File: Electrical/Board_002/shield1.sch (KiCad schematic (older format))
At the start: 12 parts, among them J1 Conn_01x02, J2 RJ45, P1 Power, P2 Analog, P3 Digital, P4 Digital, P5 CONN_01X01, P6 CONN_01X01, P7 CONN_01X01, P8 CONN_01X01

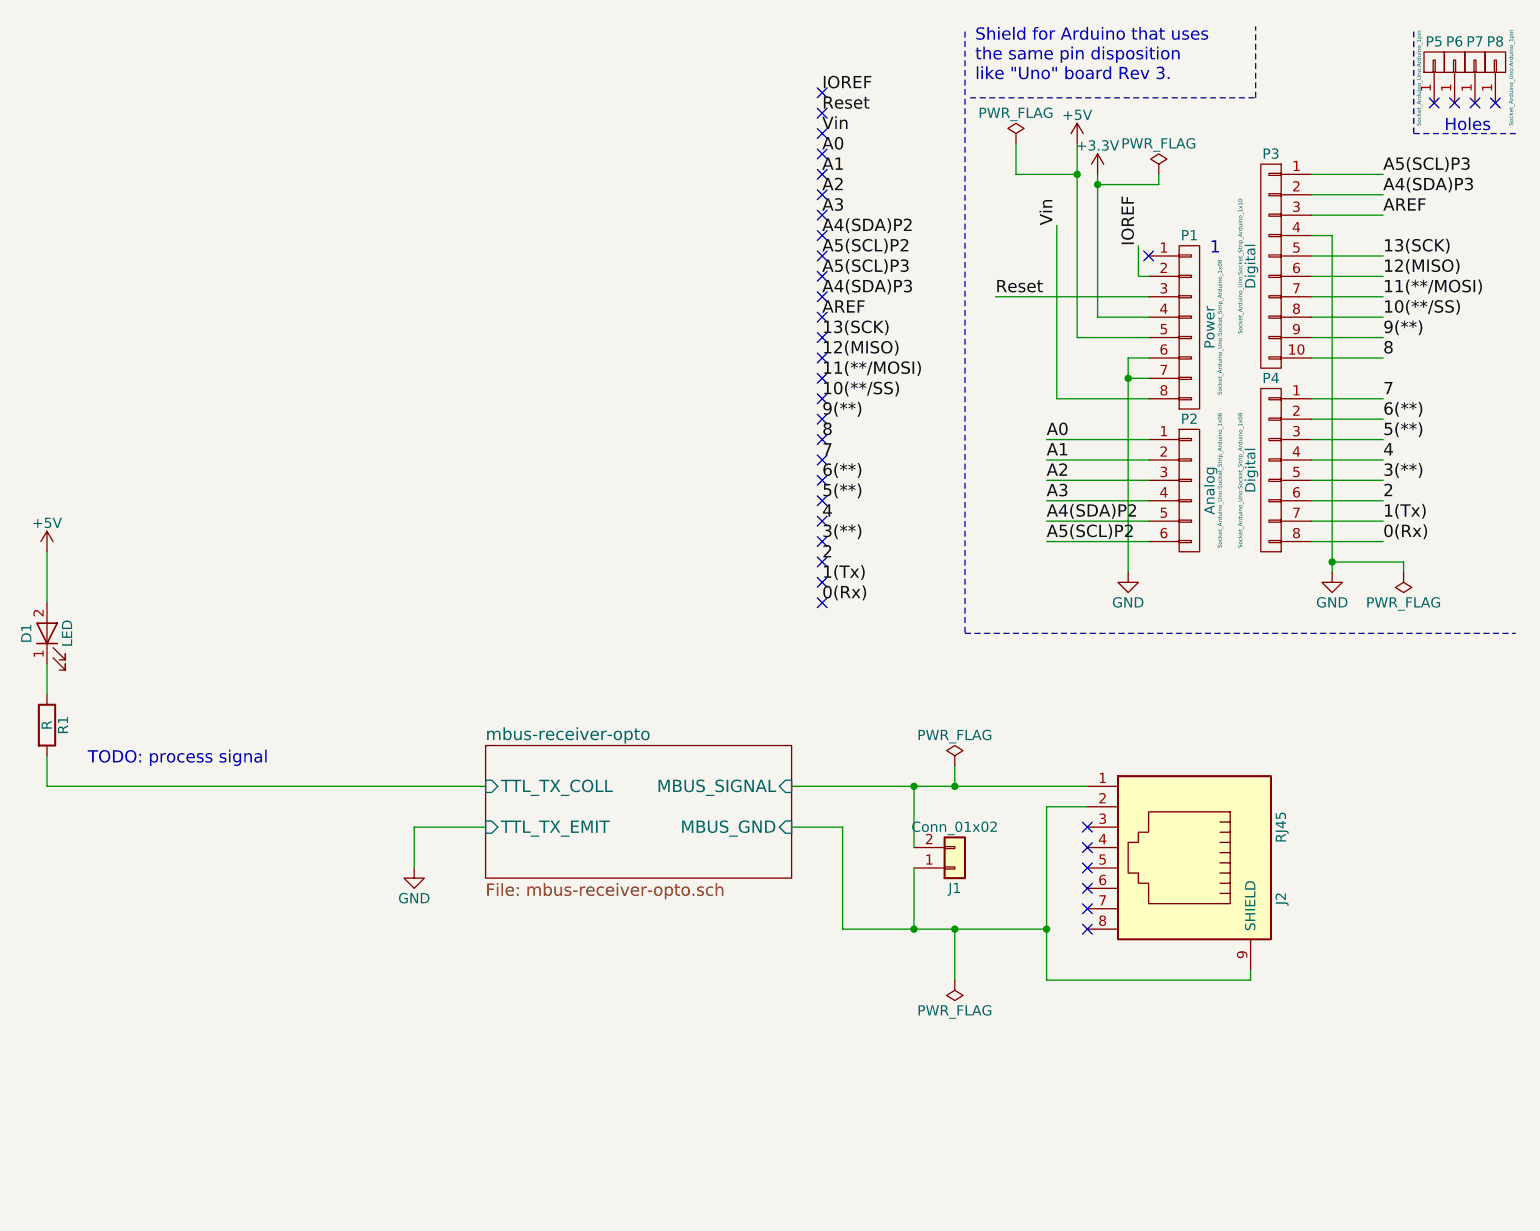
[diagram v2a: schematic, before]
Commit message: Board_002: Add mbus part border drawing
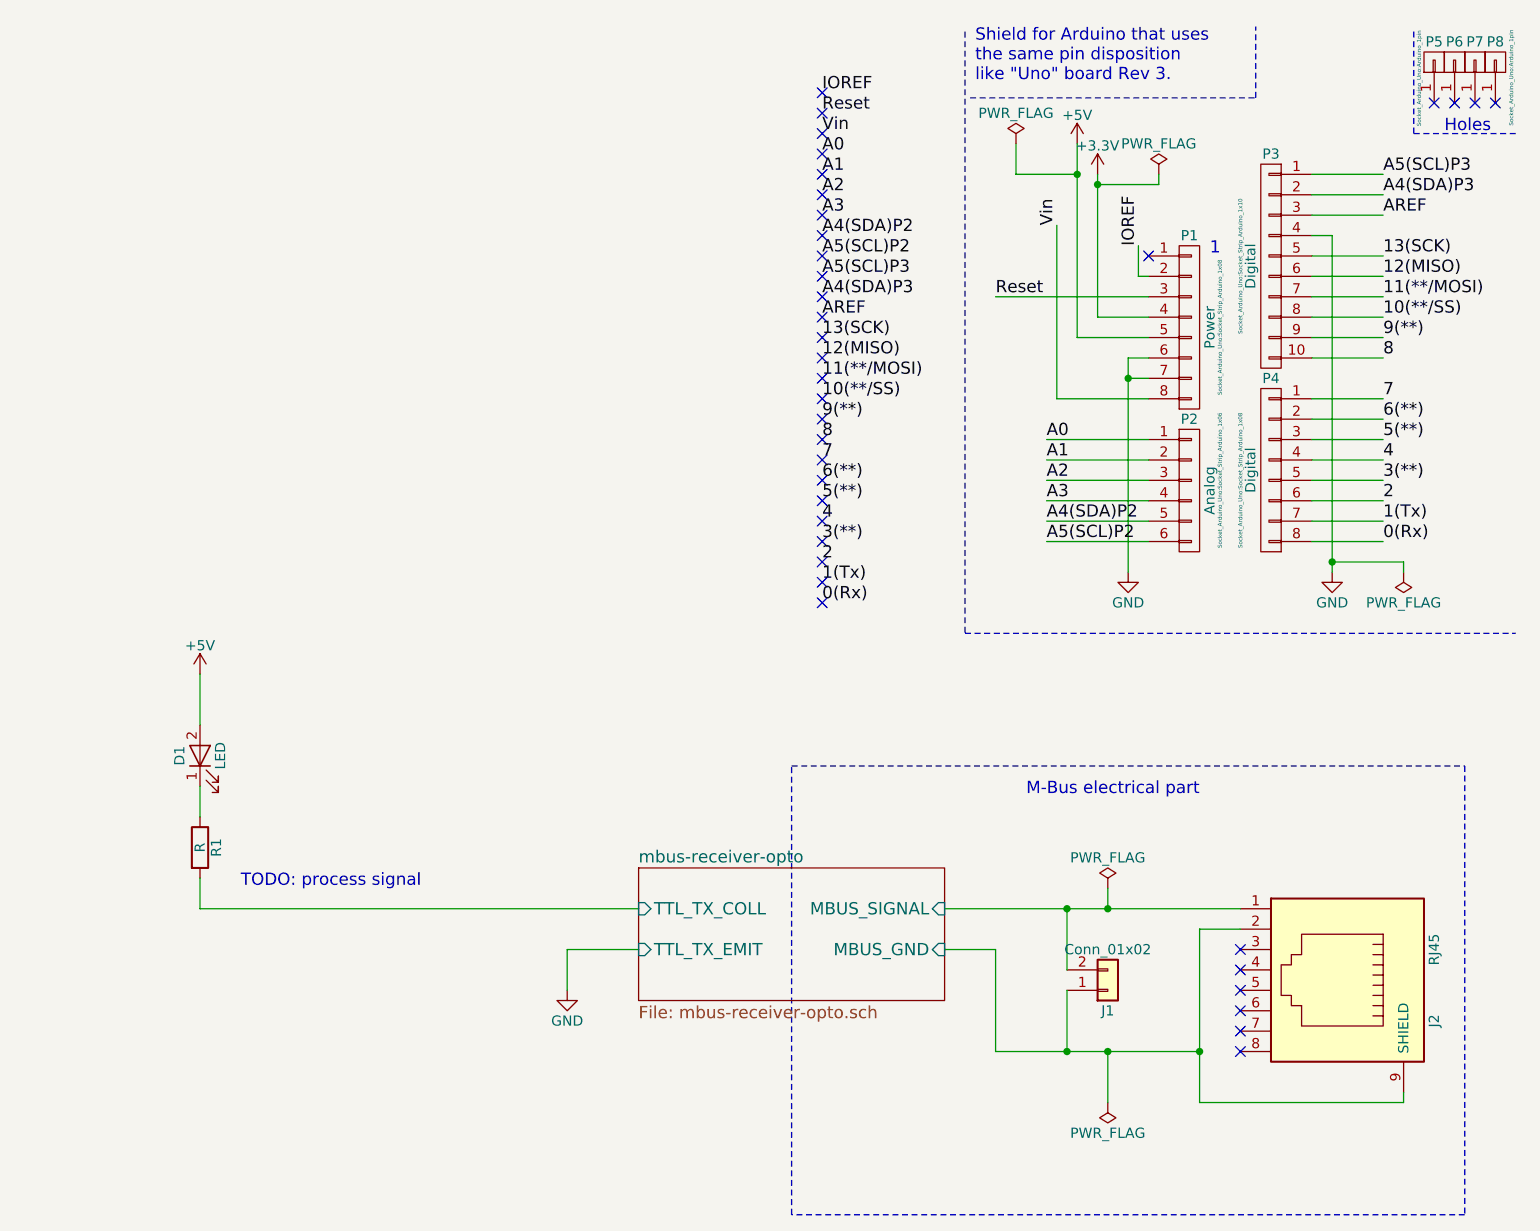
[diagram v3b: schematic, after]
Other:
- note added: "M-Bus electrical part"
- moved on the sheet: D1, J1, J2, R1
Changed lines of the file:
@@
 L RJ45 J2
 U 1 1 5A5E7E25
-P 9550 4550
-F 0 "J2" H 9750 5050 50  0000 C CNN
-F 1 "RJ45" H 9400 5050 50  0000 C CNN
-F 2 "" H 9550 4550 50  0001 C CNN
-F 3 "" H 9550 4550 50  0001 C CNN
-	1    9550 4550
+P 10300 5150
+F 0 "J2" H 10500 5650 50  0000 C CNN
+F 1 "RJ45" H 10150 5650 50  0000 C CNN
+F 2 "" H 10300 5150 50  0001 C CNN
+F 3 "" H 10300 5150 50  0001 C CNN
+	1    10300 5150
 	0    1    1    0
 $EndComp
-NoConn ~ 9100 4900
-NoConn ~ 9100 4800
-NoConn ~ 9100 4700
-NoConn ~ 9100 4600
-NoConn ~ 9100 4500
-NoConn ~ 9100 4400
-$Comp
-L PWR_FLAG #FLG05
-U 1 1 5A5E8423
-P 8450 5150
-F 0 "#FLG05" H 8450 5225 50  0001 C CNN
-F 1 "PWR_FLAG" H 8450 5300 50  0000 C CNN
-F 2 "" H 8450 5150 50  0001 C CNN
-F 3 "" H 8450 5150 50  0001 C CNN
-	1    8450 5150
-	-1   0    0    1
-$EndComp
+NoConn ~ 9850 5500
+NoConn ~ 9850 5400
+NoConn ~ 9850 5300
+NoConn ~ 9850 5200
+NoConn ~ 9850 5100
+NoConn ~ 9850 5000
 $Sheet
-S 6150 4000 1500 650
+S 6900 4600 1500 650
 U 5A61003B
 F0 "mbus-receiver-opto" 60
 F1 "mbus-receiver-opto.sch" 60
-F2 "MBUS_SIGNAL" I R 7650 4200 60
-F3 "MBUS_GND" I R 7650 4400 60
-F4 "TTL_TX_COLL" I L 6150 4200 60
-F5 "TTL_TX_EMIT" I L 6150 4400 60
+F2 "MBUS_SIGNAL" I R 8400 4800 60
+F3 "MBUS_GND" I R 8400 5000 60
+F4 "TTL_TX_COLL" I L 6900 4800 60
+F5 "TTL_TX_EMIT" I L 6900 5000 60
 $EndSheet
 $Comp
 L LED D1
 U 1 1 5A611116
-P 4000 3450
-F 0 "D1" H 4000 3550 50  0000 C CNN
-F 1 "LED" H 4000 3350 50  0000 C CNN
-F 2 "" H 4000 3450 50  0001 C CNN
-F 3 "" H 4000 3450 50  0001 C CNN
-	1    4000 3450
+P 4750 4050
+F 0 "D1" H 4750 4150 50  0000 C CNN
+F 1 "LED" H 4750 3950 50  0000 C CNN
+F 2 "" H 4750 4050 50  0001 C CNN
+F 3 "" H 4750 4050 50  0001 C CNN
+	1    4750 4050
 	0    -1   -1   0
 $EndComp
 $Comp
-L GND #PWR06
+L GND #PWR05
 U 1 1 5A6111BC
-P 5800 4600
-F 0 "#PWR06" H 5800 4350 50  0001 C CNN
-F 1 "GND" H 5800 4450 50  0000 C CNN
-F 2 "" H 5800 4600 50  0001 C CNN
-F 3 "" H 5800 4600 50  0001 C CNN
-	1    5800 4600
+P 6550 5200
+F 0 "#PWR05" H 6550 4950 50  0001 C CNN
+F 1 "GND" H 6550 5050 50  0000 C CNN
+F 2 "" H 6550 5200 50  0001 C CNN
+F 3 "" H 6550 5200 50  0001 C CNN
+	1    6550 5200
 	1    0    0    -1
 $EndComp
@@
 L R R1
 U 1 1 5A6112A2
-P 4000 3900
-F 0 "R1" V 4080 3900 50  0000 C CNN
-F 1 "R" V 4000 3900 50  0000 C CNN
-F 2 "" V 3930 3900 50  0001 C CNN
-F 3 "" H 4000 3900 50  0001 C CNN
-	1    4000 3900
-	1    0    0    -1
-$EndComp
-Text Notes 4200 4100 0    60   ~ 0
+P 4750 4500
+F 0 "R1" V 4830 4500 50  0000 C CNN
+F 1 "R" V 4750 4500 50  0000 C CNN
+F 2 "" V 4680 4500 50  0001 C CNN
+F 3 "" H 4750 4500 50  0001 C CNN
+	1    4750 4500
+	1    0    0    -1
+$EndComp
+Text Notes 4950 4700 0    60   ~ 0
 TODO: process signal
 $Comp
-L +5V #PWR07
+L +5V #PWR06
 U 1 1 5A617628
-P 4000 3050
-F 0 "#PWR07" H 4000 2900 50  0001 C CNN
-F 1 "+5V" H 4000 3190 50  0000 C CNN
-F 2 "" H 4000 3050 50  0000 C CNN
-F 3 "" H 4000 3050 50  0000 C CNN
-	1    4000 3050
+P 4750 3650
+F 0 "#PWR06" H 4750 3500 50  0001 C CNN
+F 1 "+5V" H 4750 3790 50  0000 C CNN
+F 2 "" H 4750 3650 50  0000 C CNN
+F 3 "" H 4750 3650 50  0000 C CNN
+	1    4750 3650
 	1    0    0    -1
 $EndComp
@@
 NoConn ~ 7800 800
 $Comp
-L PWR_FLAG #FLG08
+L PWR_FLAG #FLG07
 U 1 1 5A61ACC7
 P 10650 3150
-F 0 "#FLG08" H 10650 3225 50  0001 C CNN
+F 0 "#FLG07" H 10650 3225 50  0001 C CNN
 F 1 "PWR_FLAG" H 10650 3300 50  0000 C CNN
 F 2 "" H 10650 3150 50  0001 C CNN
@@
 $EndComp
 $Comp
-L PWR_FLAG #FLG09
+L PWR_FLAG #FLG08
 U 1 1 5A61AF44
 P 8750 1050
-F 0 "#FLG09" H 8750 1125 50  0001 C CNN
+F 0 "#FLG08" H 8750 1125 50  0001 C CNN
 F 1 "PWR_FLAG" H 8750 1200 50  0000 C CNN
 F 2 "" H 8750 1050 50  0001 C CNN
@@
 $EndComp
 $Comp
-L PWR_FLAG #FLG010
+L PWR_FLAG #FLG09
 U 1 1 5A61AFF4
 P 9450 1200
-F 0 "#FLG010" H 9450 1275 50  0001 C CNN
+F 0 "#FLG09" H 9450 1275 50  0001 C CNN
 F 1 "PWR_FLAG" H 9450 1350 50  0000 C CNN
 F 2 "" H 9450 1200 50  0001 C CNN
@@
 	10700 1000 10700 500
 Wire Wire Line
-	7650 4200 9100 4200
-Wire Wire Line
-	9100 4300 8900 4300
-Wire Wire Line
-	8900 4300 8900 5150
-Wire Wire Line
-	8900 5150 9900 5150
-Wire Wire Line
-	7900 4900 8900 4900
-Connection ~ 8900 4900
-Wire Wire Line
-	4000 3600 4000 3750
-Wire Wire Line
-	4000 4050 4000 4200
-Wire Wire Line
-	6150 4400 5800 4400
-Wire Wire Line
-	5800 4400 5800 4600
-Wire Wire Line
-	4000 4200 6150 4200
-Wire Wire Line
-	4000 3050 4000 3300
+	8400 4800 9850 4800
+Wire Wire Line
+	9850 4900 9650 4900
+Wire Wire Line
+	9650 4900 9650 5750
+Wire Wire Line
+	9650 5750 10650 5750
+Wire Wire Line
+	8650 5500 9650 5500
+Connection ~ 9650 5500
+Wire Wire Line
+	4750 4200 4750 4350
+Wire Wire Line
+	4750 4650 4750 4800
+Wire Wire Line
+	6900 5000 6550 5000
+Wire Wire Line
+	6550 5000 6550 5200
+Wire Wire Line
+	4750 4800 6900 4800
+Wire Wire Line
+	4750 3650 4750 3900
 Wire Wire Line
 	10650 3150 10650 3100
@@
 A4(SDA)P3
 $Comp
-L PWR_FLAG #FLG011
+L PWR_FLAG #FLG010
 U 1 1 5A61CDCA
-P 8450 4100
-F 0 "#FLG011" H 8450 4175 50  0001 C CNN
-F 1 "PWR_FLAG" H 8450 4250 50  0000 C CNN
-F 2 "" H 8450 4100 50  0001 C CNN
-F 3 "" H 8450 4100 50  0001 C CNN
-	1    8450 4100
-	1    0    0    -1
-$EndComp
-Wire Wire Line
-	8450 4100 8450 4200
-Connection ~ 8450 4200
-Wire Wire Line
-	9900 5150 9900 5100
-Wire Wire Line
-	8450 5150 8450 4900
-Connection ~ 8450 4900
+P 9200 4700
+F 0 "#FLG010" H 9200 4775 50  0001 C CNN
+F 1 "PWR_FLAG" H 9200 4850 50  0000 C CNN
+F 2 "" H 9200 4700 50  0001 C CNN
+F 3 "" H 9200 4700 50  0001 C CNN
+	1    9200 4700
+	1    0    0    -1
+$EndComp
+Wire Wire Line
+	9200 4700 9200 4800
+Connection ~ 9200 4800
+Wire Wire Line
+	10650 5750 10650 5700
 $Comp
 L Conn_01x02 J1
 U 1 1 5A627909
-P 8450 4600
-F 0 "J1" H 8450 4700 50  0000 C CNN
-F 1 "Conn_01x02" H 8450 4400 50  0000 C CNN
-F 2 "" H 8450 4600 50  0001 C CNN
-F 3 "" H 8450 4600 50  0001 C CNN
-	1    8450 4600
+P 9200 5200
+F 0 "J1" H 9200 5300 50  0000 C CNN
+F 1 "Conn_01x02" H 9200 5000 50  0000 C CNN
+F 2 "" H 9200 5200 50  0001 C CNN
+F 3 "" H 9200 5200 50  0001 C CNN
+	1    9200 5200
 	1    0    0    1
 $EndComp
 Wire Wire Line
-	7650 4400 7900 4400
-Wire Wire Line
-	7900 4400 7900 4900
-Wire Wire Line
-	8250 4600 8250 4900
-Connection ~ 8250 4900
-Wire Wire Line
-	8250 4500 8250 4200
-Connection ~ 8250 4200
+	8400 5000 8650 5000
+Wire Wire Line
+	8650 5000 8650 5500
+Wire Wire Line
+	9000 5200 9000 5500
+Connection ~ 9000 5500
+Wire Wire Line
+	9000 5100 9000 4800
+Connection ~ 9000 4800
+Wire Notes Line
+	7650 4100 10950 4100
+Wire Notes Line
+	10950 4100 10950 6300
+Wire Notes Line
+	10950 6300 7650 6300
+Wire Notes Line
+	7650 6300 7650 4100
+Text Notes 8800 4250 0    60   ~ 0
+M-Bus electrical part
+Connection ~ 9200 5500
+Wire Wire Line
+	9200 5750 9200 5500
+$Comp
+L PWR_FLAG #FLG011
+U 1 1 5A5E8423
+P 9200 5750
+F 0 "#FLG011" H 9200 5825 50  0001 C CNN
+F 1 "PWR_FLAG" H 9200 5900 50  0000 C CNN
+F 2 "" H 9200 5750 50  0001 C CNN
+F 3 "" H 9200 5750 50  0001 C CNN
+	1    9200 5750
+	-1   0    0    1
+$EndComp
 $EndSCHEMATC
